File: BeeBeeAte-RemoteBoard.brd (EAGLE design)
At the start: 59 x 85 mm, 56 parts, among them IC1 CP2102, J1 3-1734035-2, T1 S8050, T2 S8050, U1 ESP32-WROOM-32, U2 LM5.0

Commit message: Added Logo to remote and created GERBER, BOM and CPL for remote
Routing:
- net 3V3: track 209.6 -> 208.2 mm
- net VRY: track 68.9 -> 69.6 mm

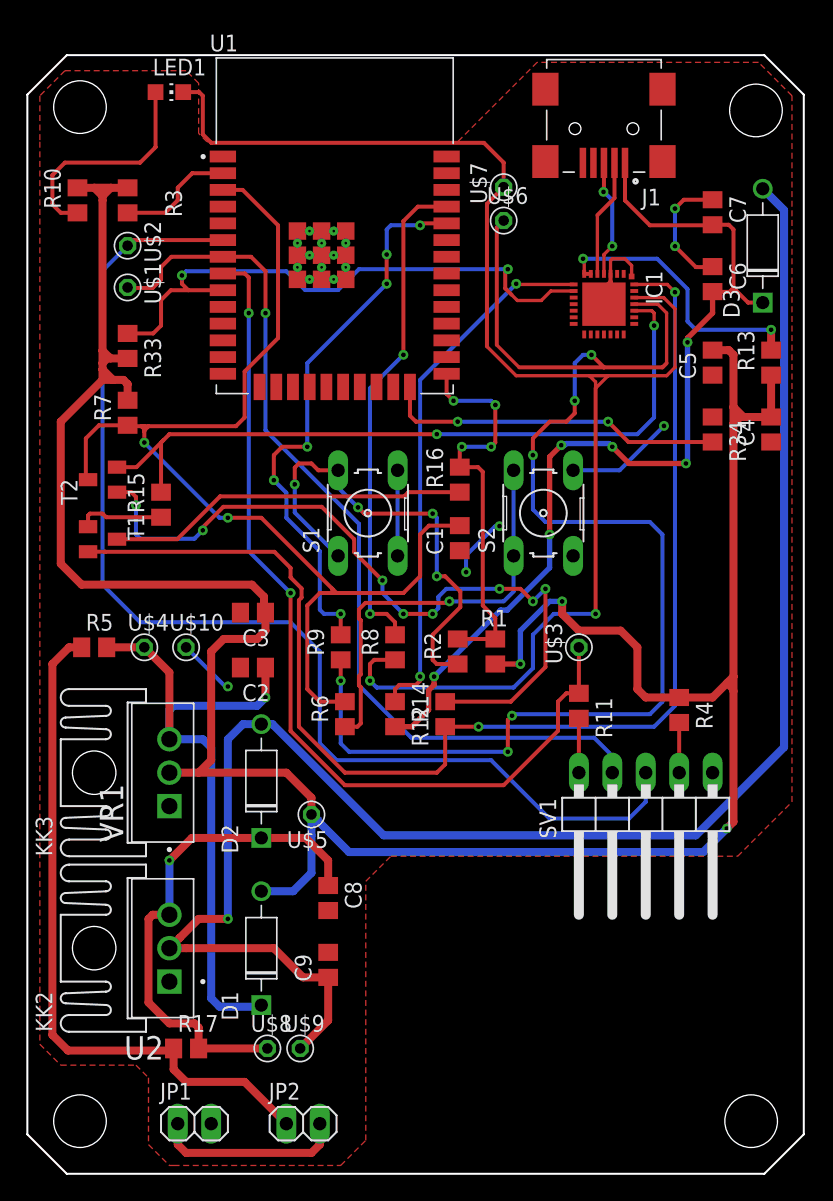
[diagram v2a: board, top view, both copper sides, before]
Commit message: Added 3D Files and modified Board
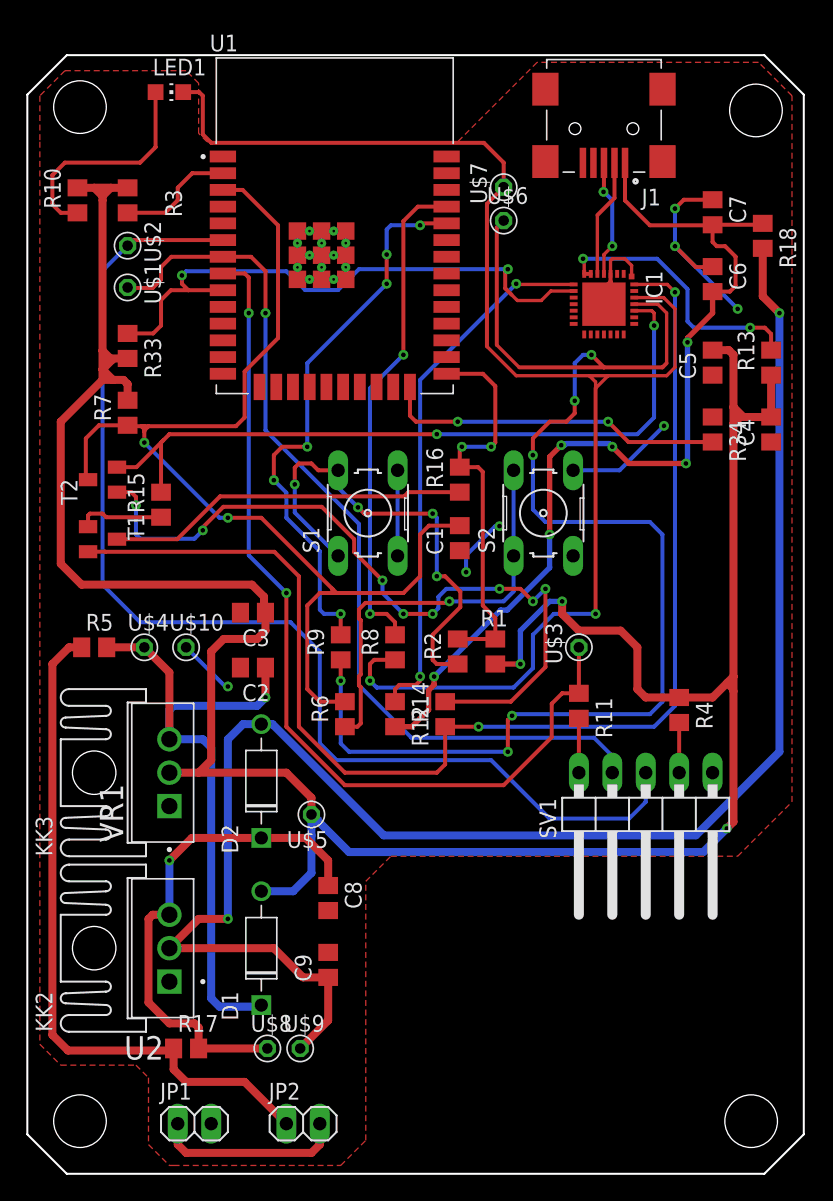
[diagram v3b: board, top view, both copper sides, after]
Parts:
- removed D3: 1N4007, Diodes:DO-41
- added R18: 0, rcl:R0805
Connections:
- net 5V: now also R18.2; no longer D3.A
- net VBUS: now also R18.1; no longer D3.C
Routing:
- net GND: track 40.5 -> 47.3 mm, vias 6 -> 7
- net 5V: track 130.4 -> 125.6 mm, vias 1 -> 2
- net VBUS: track 72.9 -> 73.5 mm
- net 3V3: track 208.2 -> 208.7 mm
- net PIN0: track 30.6 -> 30.5 mm, vias 4 -> 2

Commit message: Checked by teacher and fixed
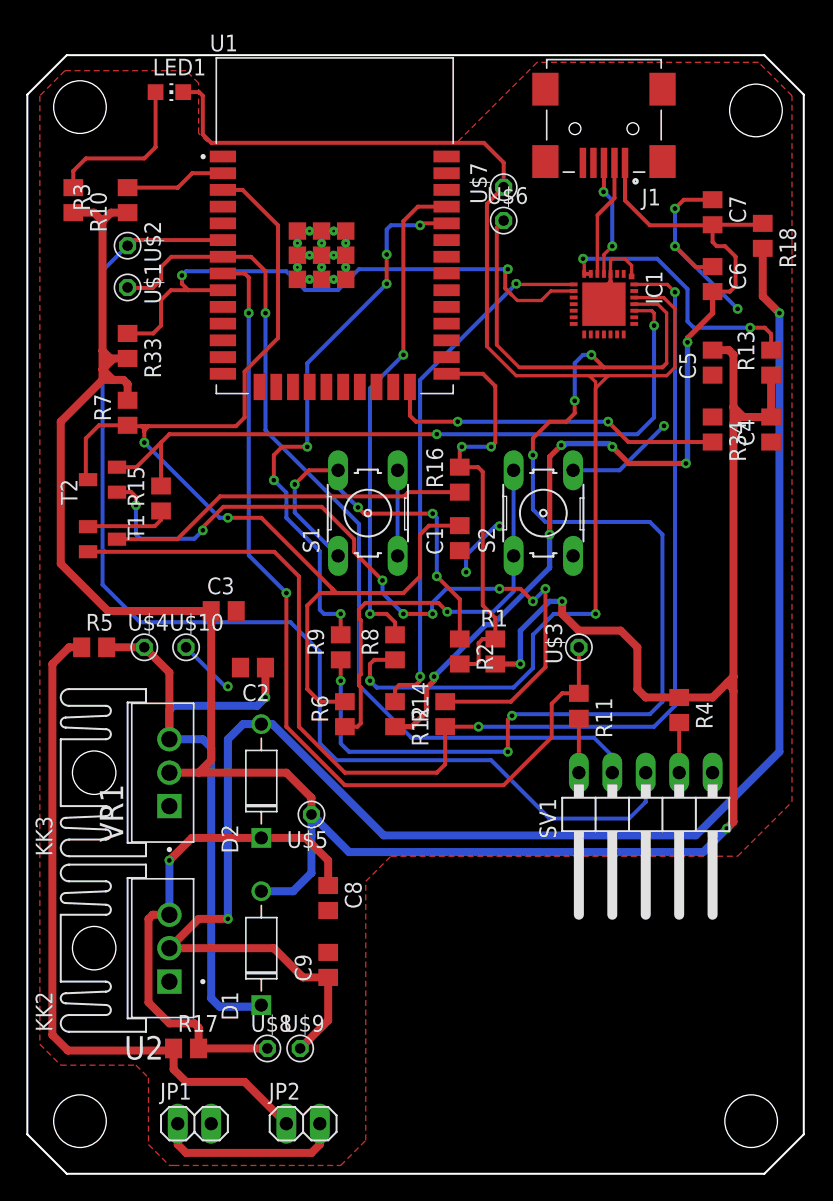
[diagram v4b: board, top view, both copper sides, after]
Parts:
- moved C3 2.23 mm to (14.9, 42.8), turned to 0 degrees
- moved R15 0.48 mm to (10.2, 51.3)
- moved R10 0.32 mm to (3.49, 74.0), turned to 270 degrees
- moved R2 0.16 mm to (32.9, 39.7), turned to 270 degrees
- turned R3 to 270 degrees
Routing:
- net 3V3: track 208.7 -> 198.0 mm
- net N$1: track 36.3 -> 30.2 mm
- net N$7: track 17.3 -> 12.5 mm
- net PIN0: track 30.5 -> 32.0 mm
- net N$15: track 9.04 -> 7.70 mm
- net N$2: track 31.7 -> 32.2 mm
